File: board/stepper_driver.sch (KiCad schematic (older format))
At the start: 28 parts

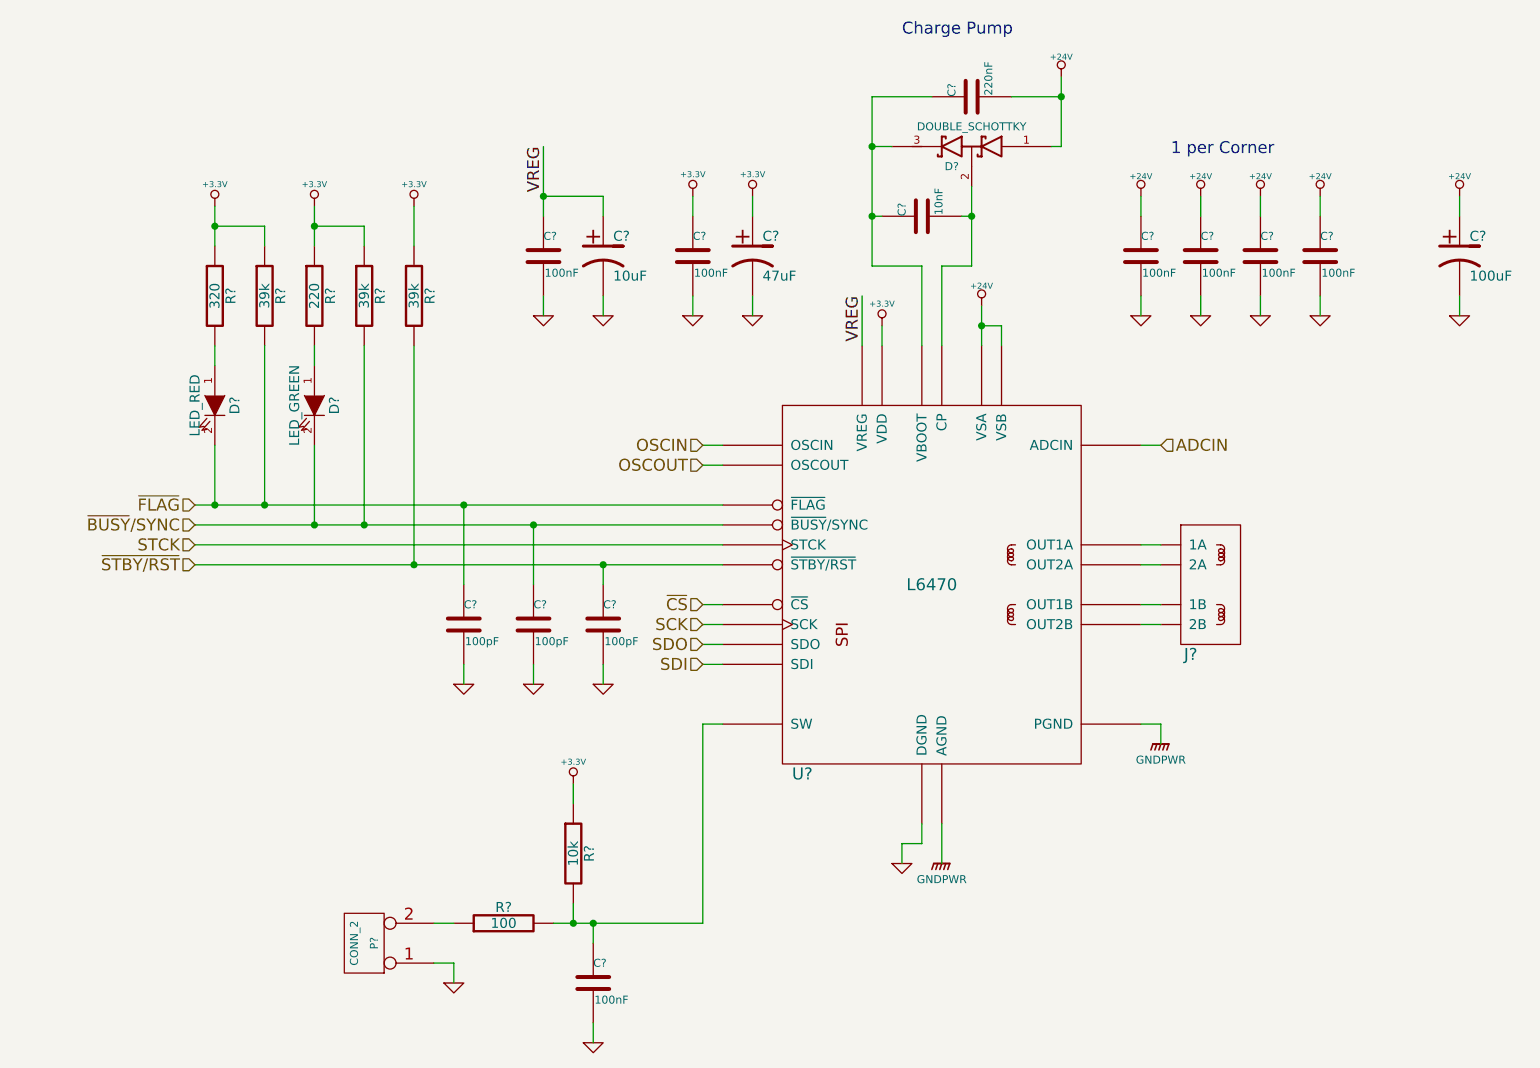
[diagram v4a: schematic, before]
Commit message: Fixed ERC Errors. Annotated all components.
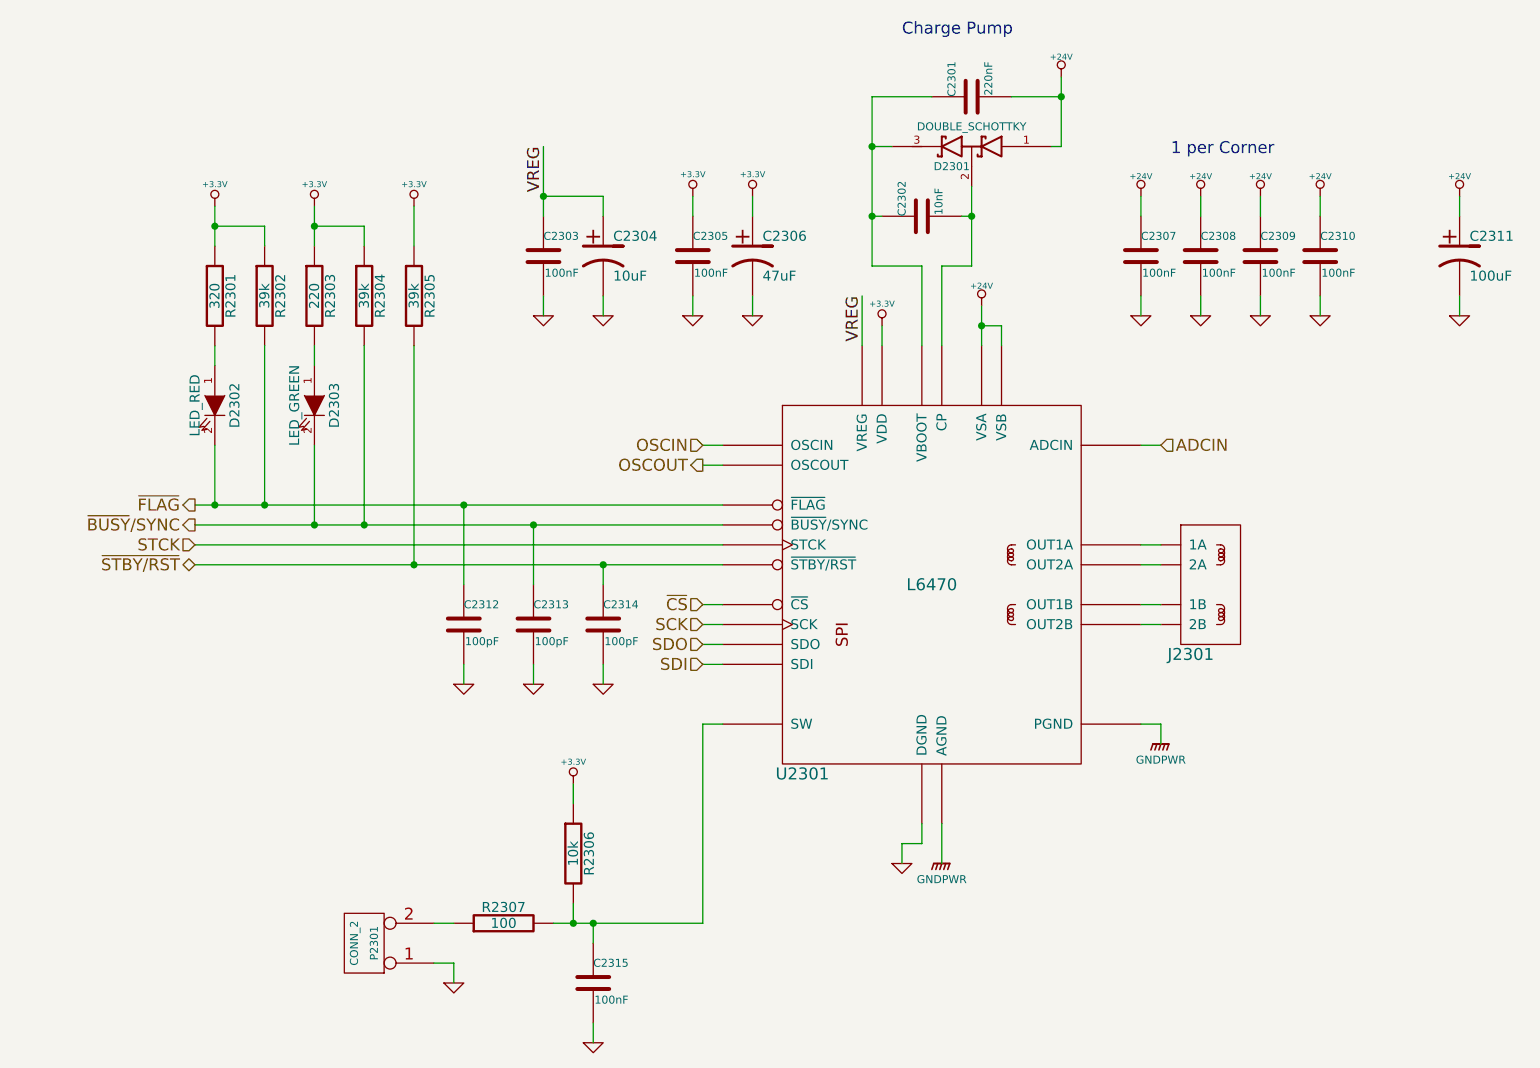
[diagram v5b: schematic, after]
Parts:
- gave numbers to parts that had none: 28
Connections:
- new net: J2301.~ (2B), U2301.~ (~STBY/RST) (x3)
